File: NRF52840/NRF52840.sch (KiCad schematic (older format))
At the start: 28 parts, among them Y1 32Mhz, Y2 32.768kHz

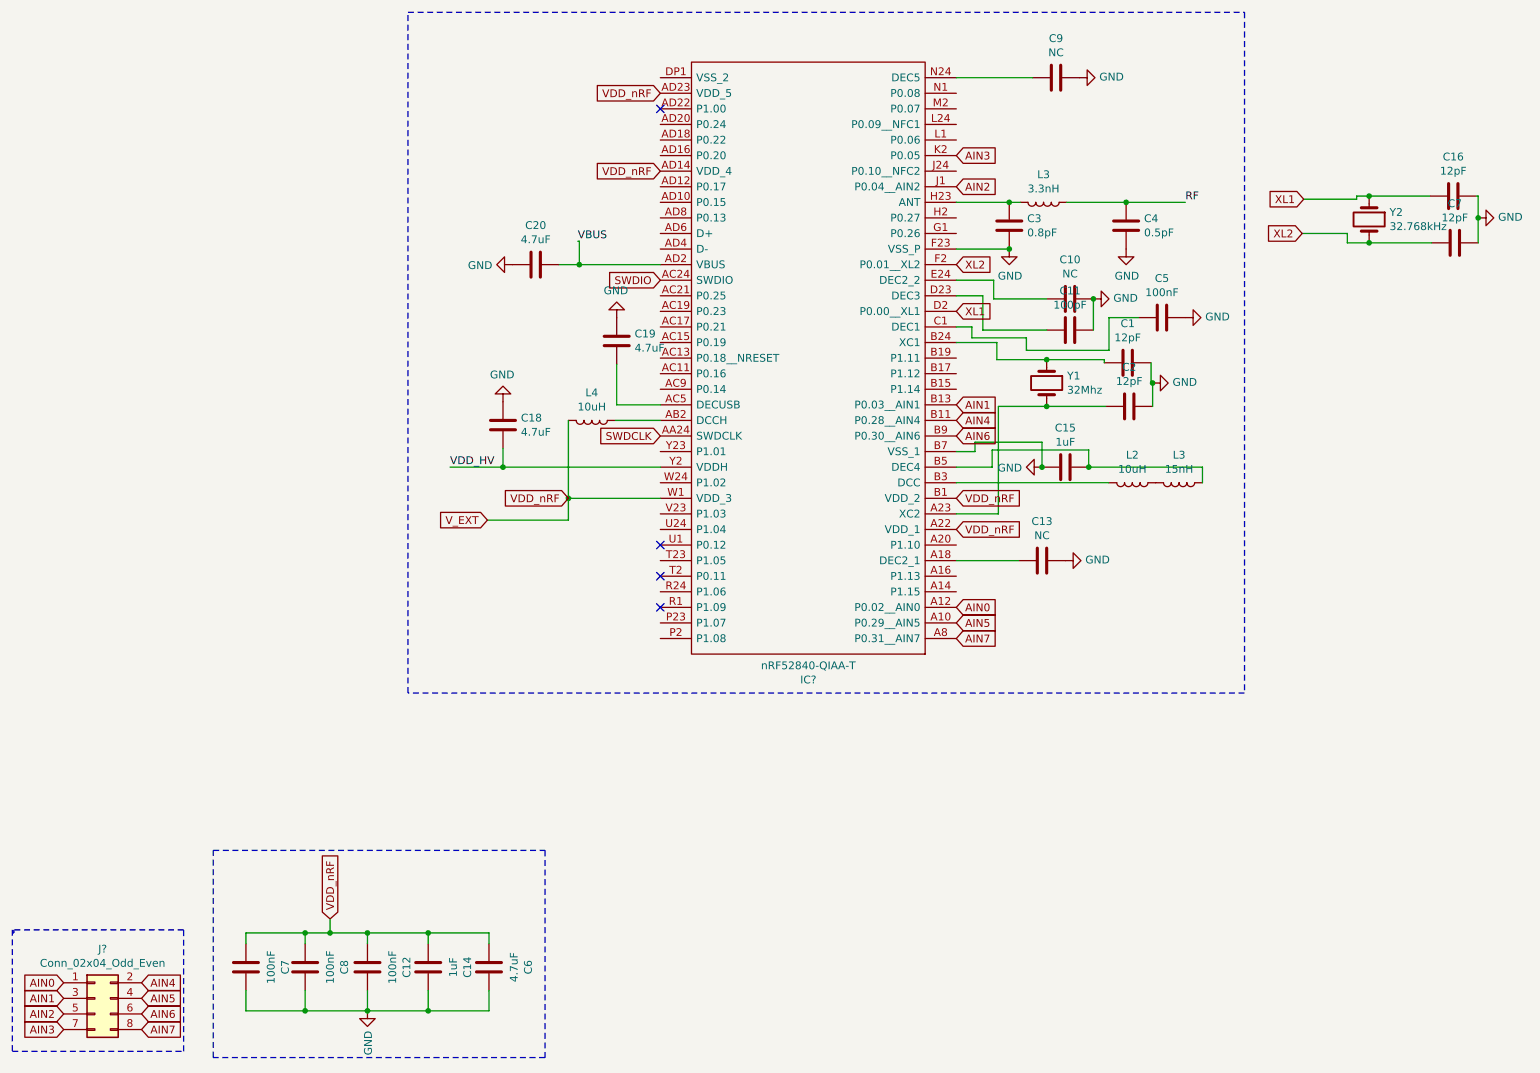
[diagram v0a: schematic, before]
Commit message: added GPIO and SWD/JTAG connector
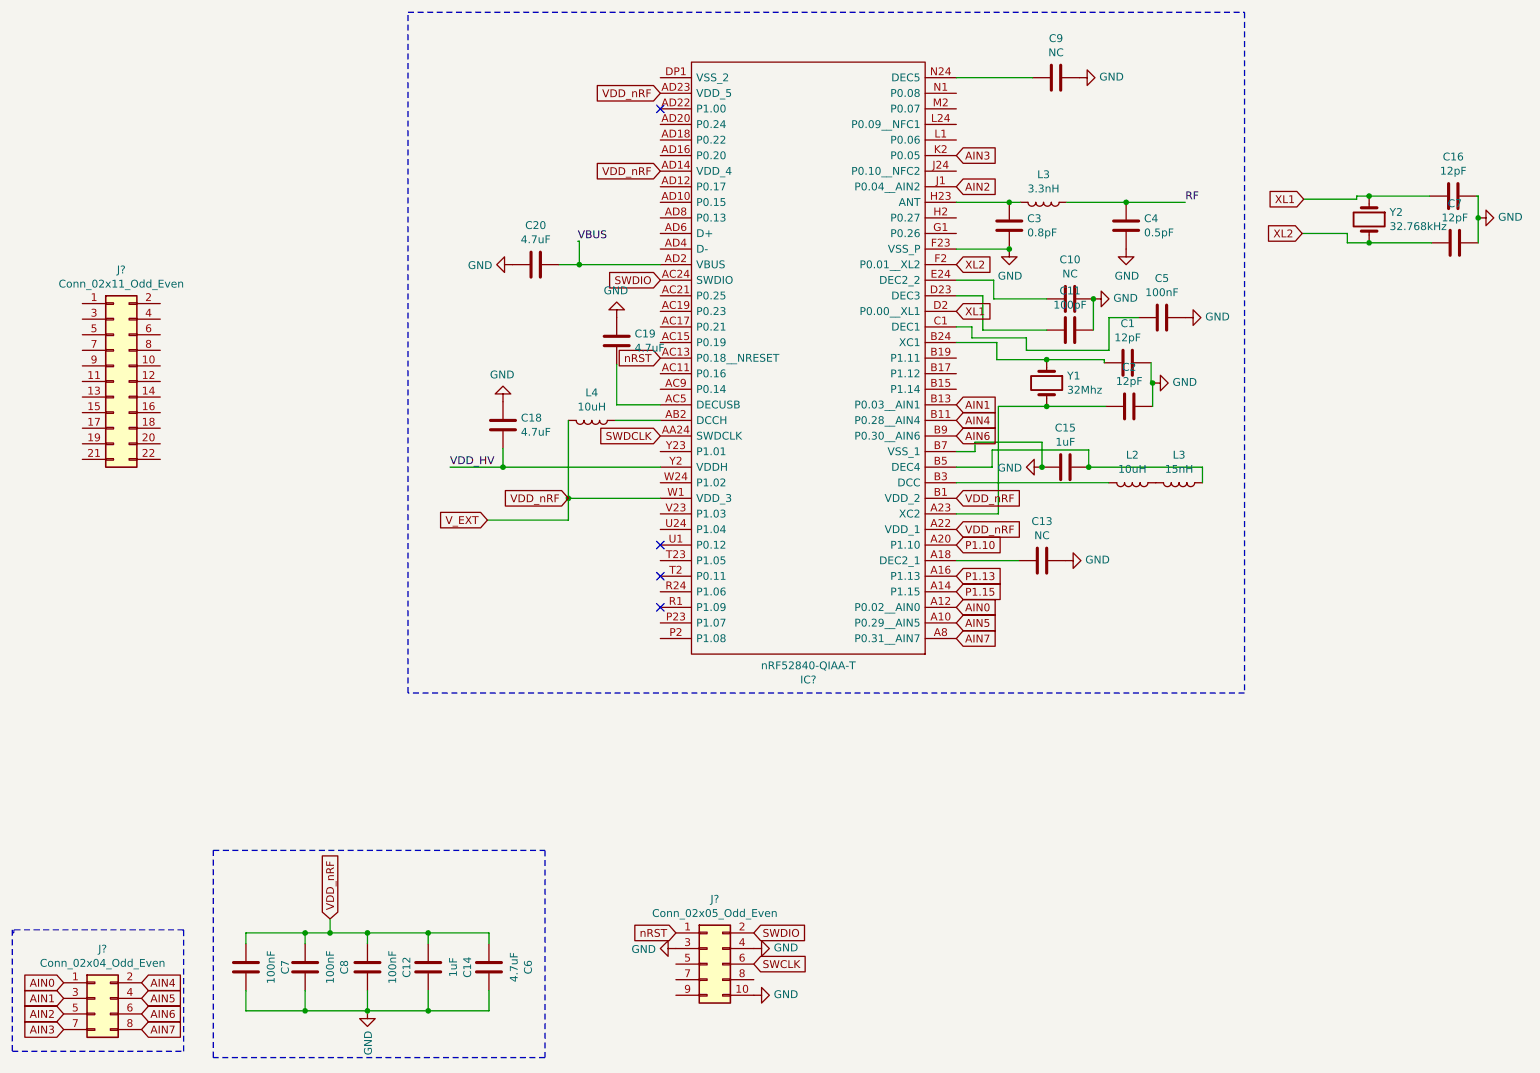
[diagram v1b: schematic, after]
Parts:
- added J?: Conn_02x05_Odd_Even, symbol Connector_Generic:Conn_02x05_Odd_Even
- added J?: Conn_02x11_Odd_Even, symbol Connector_Generic:Conn_02x11_Odd_Even
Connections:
- net GND: now also J?.10 (Pin_10), J?.3 (Pin_3), J?.4 (Pin_4)
- net SWDIO: now also J?.2 (Pin_2)
- net P1.15: now reaches IC?.A14 (P1.15)
- net P1.13: now reaches IC?.A16 (P1.13)
- net P1.10: now reaches IC?.A20 (P1.10)
- net nRST: now reaches IC?.AC13 (P0.18__NRESET)
- net nRST: now also J?.1 (Pin_1)
- new net SWCLK: J?.6 (Pin_6)
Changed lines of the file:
@@
 NoConn ~ 4780 4400
 NoConn ~ 4780 1600
+Text GLabel 4780 3200 0    50   Input ~ 0
+nRST
+$Comp
+L Connector_Generic:Conn_02x05_Odd_Even J?
+U 1 1 5C8B25FA
+P 5080 7090
+F 0 "J?" H 5130 7507 50  0000 C CNN
+F 1 "Conn_02x05_Odd_Even" H 5130 7416 50  0000 C CNN
+F 2 "" H 5080 7090 50  0001 C CNN
+F 3 "~" H 5080 7090 50  0001 C CNN
+	1    5080 7090
+	1    0    0    -1
+$EndComp
+Text GLabel 5380 6890 2    50   Input ~ 0
+SWDIO
+Text GLabel 5380 7090 2    50   Input ~ 0
+SWCLK
+$Comp
+L power:GND #PWR?
+U 1 1 5C8B294C
+P 5380 6990
+F 0 "#PWR?" H 5380 6740 50  0001 C CNN
+F 1 "GND" V 5385 6862 50  0000 R CNN
+F 2 "" H 5380 6990 50  0001 C CNN
+F 3 "" H 5380 6990 50  0001 C CNN
+	1    5380 6990
+	0    -1   -1   0
+$EndComp
+$Comp
+L power:GND #PWR?
+U 1 1 5C8B2993
+P 5380 7290
+F 0 "#PWR?" H 5380 7040 50  0001 C CNN
+F 1 "GND" V 5385 7162 50  0000 R CNN
+F 2 "" H 5380 7290 50  0001 C CNN
+F 3 "" H 5380 7290 50  0001 C CNN
+	1    5380 7290
+	0    -1   -1   0
+$EndComp
+Text GLabel 4880 6890 0    50   Input ~ 0
+nRST
+$Comp
+L power:GND #PWR?
+U 1 1 5C8B2B26
+P 4880 6990
+F 0 "#PWR?" H 4880 6740 50  0001 C CNN
+F 1 "GND" V 4885 6862 50  0000 R CNN
+F 2 "" H 4880 6990 50  0001 C CNN
+F 3 "" H 4880 6990 50  0001 C CNN
+	1    4880 6990
+	0    1    1    0
+$EndComp
+$Comp
+L Connector_Generic:Conn_02x11_Odd_Even J?
+U 1 1 5C8B8E2E
+P 1270 3350
+F 0 "J?" H 1320 4067 50  0000 C CNN
+F 1 "Conn_02x11_Odd_Even" H 1320 3976 50  0000 C CNN
+F 2 "" H 1270 3350 50  0001 C CNN
+F 3 "~" H 1270 3350 50  0001 C CNN
+	1    1270 3350
+	1    0    0    -1
+$EndComp
+Text GLabel 6680 4700 2    50   Input ~ 0
+P1.15
+Text GLabel 6680 4600 2    50   Input ~ 0
+P1.13
+Text GLabel 6680 4400 2    50   Input ~ 0
+P1.10
 $EndSCHEMATC

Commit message: footprint assignment to components
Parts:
- C1, C10, C11, C12, C13, C16, C18, C19, C2, C3, C4, C5, C7, C8, C9: footprint (none) -> Capacitor_SMD:C_0402_1005Metric
- C14, C15, C20, C6: footprint (none) -> Capacitor_SMD:C_0603_1608Metric
- C25: renamed from C7; footprint (none) -> Capacitor_SMD:C_0402_1005Metric
- IC1: renamed from IC?; footprint AQFN73 -> User_library:AQFN73
- J1: renamed from J?; footprint (none) -> Connector_PinHeader_2.00mm:PinHeader_2x04_P2.00mm_Vertical
- J2: renamed from J?; footprint (none) -> Connector_PinHeader_2.00mm:PinHeader_2x11_P2.00mm_Vertical
- J3: renamed from J?; footprint (none) -> Connector_PinHeader_2.00mm:PinHeader_2x05_P2.00mm_Vertical
- L2, L3, L4: footprint (none) -> Inductor_SMD:L_0402_1005Metric
- L5: renamed from L3; footprint (none) -> Inductor_SMD:L_0402_1005Metric
- Y1: footprint (none) -> User_library:81-XRCGB32M000F1H00R(XTAL_2016)
- Y2: footprint (none) -> Crystal:Crystal_SMD_3215-2Pin_3.2x1.5mm
